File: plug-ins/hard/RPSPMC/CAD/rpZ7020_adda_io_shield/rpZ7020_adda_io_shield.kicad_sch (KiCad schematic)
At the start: 11 parts, among them J1 Samtec_ASP-134486-01

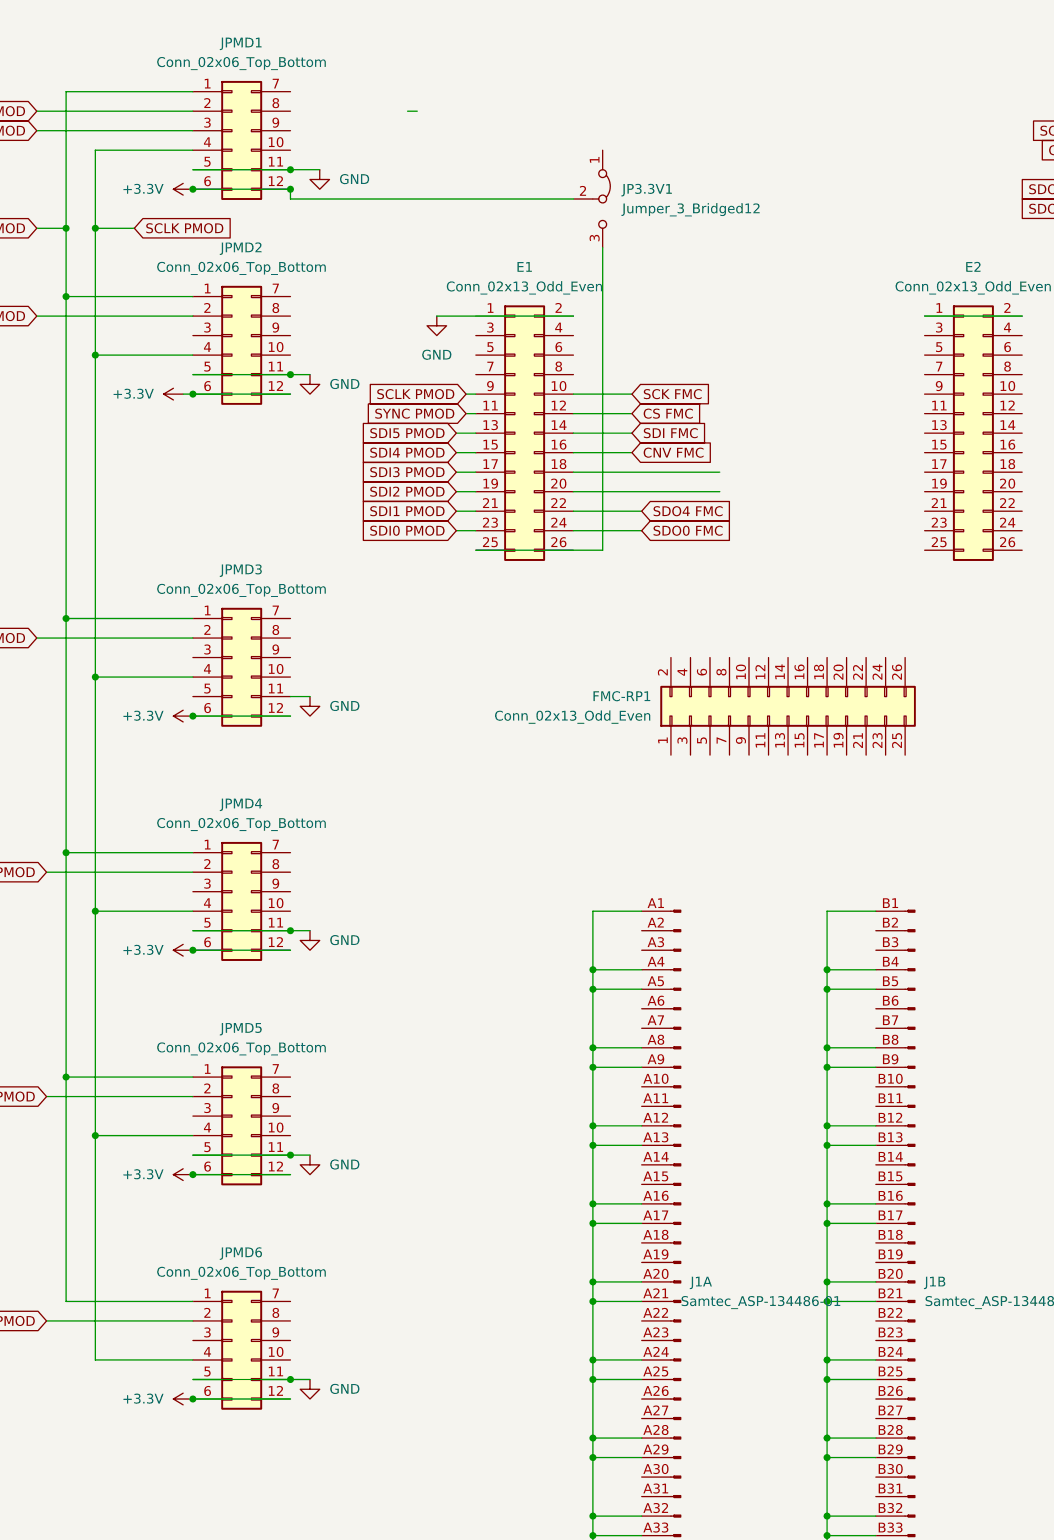
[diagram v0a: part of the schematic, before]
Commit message: profile: auto update axis labels+title from unit MUX: test modes CAD: work on RP hat
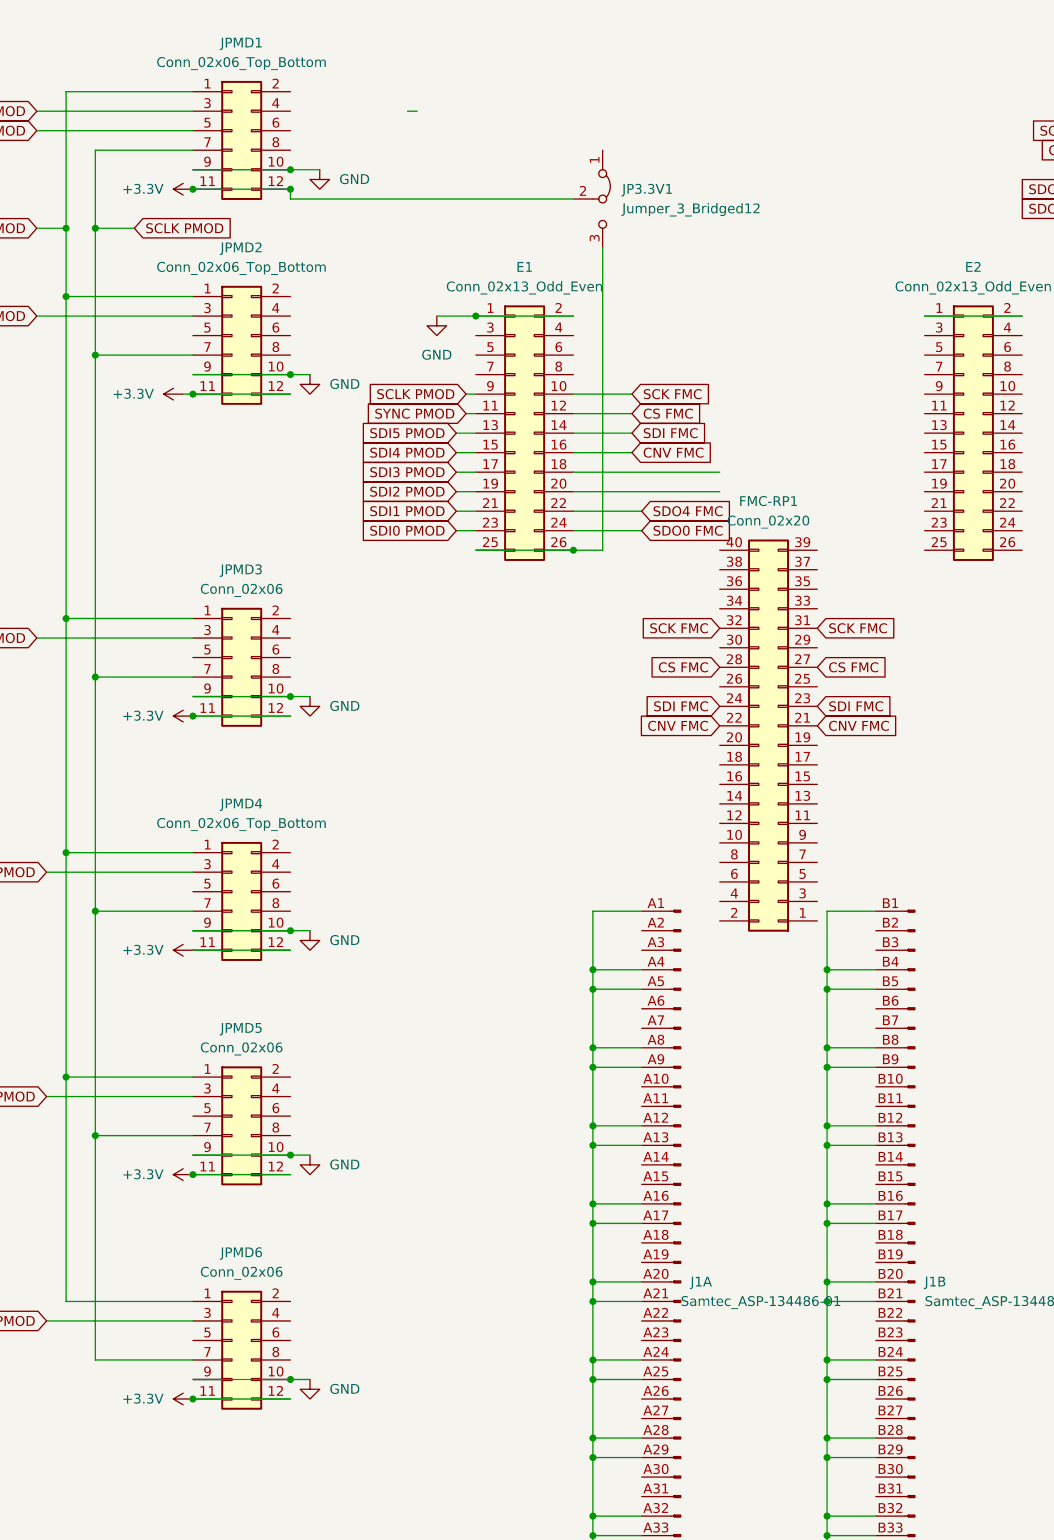
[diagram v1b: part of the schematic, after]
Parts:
- FMC-RP1: value Conn_02x13_Odd_Even -> Conn_02x20; footprint Connector_PinHeader_2.54mm:PinHeader_2x13_P2.54mm_Vertical -> Connector_PinHeader_2.54mm:PinHeader_2x20_P2.54mm_Vertical; symbol Connector_Generic:Conn_02x13_Odd_Even -> Connector_Generic:Conn_02x20_Odd_Even
- JP3.3V1: footprint (none) -> Connector_PinSocket_2.54mm:PinSocket_1x03_P2.54mm_Vertical
- JPMD1, JPMD2, JPMD4: footprint Connector_PinSocket_2.54mm:PinSocket_2x06_P2.54mm_Horizontal -> Connector_PinSocket_2.54mm:PinSocket_2x06_P2.54mm_Vertical; symbol Connector_Generic:Conn_02x06_Top_Bottom -> Connector_Generic:Conn_02x06_Odd_Even
- JPMD3, JPMD5, JPMD6: value Conn_02x06_Top_Bottom -> Conn_02x06; footprint Connector_PinSocket_2.54mm:PinSocket_2x06_P2.54mm_Horizontal -> Connector_PinSocket_2.54mm:PinSocket_2x06_P2.54mm_Vertical; symbol Connector_Generic:Conn_02x06_Top_Bottom -> Connector_Generic:Conn_02x06_Odd_Even
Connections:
- net +3.3V: now also JPMD1.11 (Pin_11), JPMD2.11 (Pin_11), JPMD3.11 (Pin_11), JPMD4.11 (Pin_11), JPMD5.11 (Pin_11), JPMD6.11 (Pin_11); no longer JPMD1.6 (Pin_6), JPMD2.6 (Pin_6), JPMD3.6 (Pin_6), JPMD4.6 (Pin_6), JPMD5.6 (Pin_6), JPMD6.6 (Pin_6)
- net CNV FMC: now also FMC-RP1.21 (Pin_21), FMC-RP1.22 (Pin_22)
- net CS FMC: now also FMC-RP1.27 (Pin_27), FMC-RP1.28 (Pin_28)
- net GND: now also E1.1 (Pin_1), JPMD1.10 (Pin_10), JPMD1.9 (Pin_9), JPMD2.10 (Pin_10), JPMD2.9 (Pin_9), JPMD3.10 (Pin_10), JPMD3.9 (Pin_9), JPMD4.10 (Pin_10), JPMD4.9 (Pin_9), JPMD5.10 (Pin_10), JPMD5.9 (Pin_9), JPMD6.10 (Pin_10), JPMD6.9 (Pin_9); no longer JPMD1.11 (Pin_11), JPMD1.5 (Pin_5), JPMD2.11 (Pin_11), JPMD2.5 (Pin_5), JPMD3.11 (Pin_11), JPMD4.11 (Pin_11), JPMD4.5 (Pin_5), JPMD5.11 (Pin_11), JPMD5.5 (Pin_5), JPMD6.11 (Pin_11), JPMD6.5 (Pin_5)
- net SCK FMC: now also FMC-RP1.31 (Pin_31), FMC-RP1.32 (Pin_32)
- net SCLK PMOD: now also JPMD1.7 (Pin_7), JPMD2.7 (Pin_7), JPMD3.7 (Pin_7), JPMD4.7 (Pin_7), JPMD5.7 (Pin_7), JPMD6.7 (Pin_7); no longer JPMD1.4 (Pin_4), JPMD2.4 (Pin_4), JPMD3.4 (Pin_4), JPMD4.4 (Pin_4), JPMD5.4 (Pin_4), JPMD6.4 (Pin_4)
- net SDI FMC: now also FMC-RP1.23 (Pin_23), FMC-RP1.24 (Pin_24)
- net SDI0 PMOD: now also JPMD1.3 (Pin_3); no longer JPMD1.2 (Pin_2)
- net SDI1 PMOD: now also JPMD2.3 (Pin_3); no longer JPMD2.2 (Pin_2)
- net SDI2 PMOD: now also JPMD3.3 (Pin_3); no longer JPMD3.2 (Pin_2)
- net SDI3 PMOD: now also JPMD4.3 (Pin_3); no longer JPMD4.2 (Pin_2)
- net SDI4 PMOD: now also JPMD5.3 (Pin_3); no longer JPMD5.2 (Pin_2)
- net SDI5 PMOD: now also JPMD6.3 (Pin_3); no longer JPMD6.2 (Pin_2)
- net SDO0 PMOD: now also JPMD1.5 (Pin_5); no longer JPMD1.3 (Pin_3)
- net at E1.25 (Pin_25), JP3.3V1.3 (B): now also E1.26 (Pin_26)

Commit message: work on RP hat
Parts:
- added C1, C2, C3, C4, C5, C6: C, Capacitor_THT:C_Rect_L4.6mm_W2.0mm_P2.50mm_MKS02_FKP02, symbol Device:C
- added J3-FMC-POWER1, J4-FMC-AUX1: Conn_02x06_Odd_Even, Connector_PinHeader_2.54mm:PinHeader_2x06_P2.54mm_Vertical, symbol Connector_Generic:Conn_02x06_Odd_Even
- added R1, R2: 1k, Resistor_SMD:R_0805_2012Metric, symbol Device:R
- JP-EXT-3.3V-RP1: renamed from JP3.3V1; footprint Connector_PinSocket_2.54mm:PinSocket_1x03_P2.54mm_Vertical -> Connector_PinHeader_2.54mm:PinHeader_1x03_P2.54mm_Vertical
- renumbered FMC-RP1 to J2-FMC-RP1
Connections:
- net +12V FMC: now also J3-FMC-POWER1.1 (Pin_1), J3-FMC-POWER1.2 (Pin_2)
- net +3.3V: now also C1.2, C2.2, C3.2, C4.2, C5.2, C6.2
- net A0 EE: now also J4-FMC-AUX1.10 (Pin_10)
- net A1 EE: now also J4-FMC-AUX1.12 (Pin_12)
- net AUX 3.3V EE: now also J3-FMC-POWER1.8 (Pin_8)
- net BUSY FMC: now also J2-FMC-RP1.19 (Pin_19)
- net CLK-ADC: now also J4-FMC-AUX1.1 (Pin_1)
- net CNV FMC: no longer E1.16 (Pin_16), J2-FMC-RP1.22 (Pin_22)
- net CS FMC: now also J2-FMC-RP1.17 (Pin_17); no longer E1.12 (Pin_12), J2-FMC-RP1.27 (Pin_27), J2-FMC-RP1.28 (Pin_28)
- net EN: now also J4-FMC-AUX1.8 (Pin_8)
- net GND: now also E2.1 (Pin_1), E2.15 (Pin_15), E2.2 (Pin_2), E2.5 (Pin_5), E2.6 (Pin_6), C1.1, C2.1, C3.1, C4.1, C5.1, C6.1, J3-FMC-POWER1.11 (Pin_11), J3-FMC-POWER1.3 (Pin_3), J3-FMC-POWER1.4 (Pin_4), J3-FMC-POWER1.5 (Pin_5), J3-FMC-POWER1.6 (Pin_6), J4-FMC-AUX1.11 (Pin_11), J4-FMC-AUX1.3 (Pin_3), J4-FMC-AUX1.4 (Pin_4), J4-FMC-AUX1.5 (Pin_5), J4-FMC-AUX1.6 (Pin_6), J4-FMC-AUX1.9 (Pin_9)
- net RESET FMC: now also J2-FMC-RP1.29 (Pin_29)
- net SCK FMC: now also J2-FMC-RP1.25 (Pin_25); no longer E1.10 (Pin_10), J2-FMC-RP1.31 (Pin_31), J2-FMC-RP1.32 (Pin_32)
- net SCK OUT FMC: now also J2-FMC-RP1.31 (Pin_31)
- net SCL EE: now also J2-FMC-RP1.37 (Pin_37)
- net SDA EE: now also J2-FMC-RP1.39 (Pin_39)
- net SDI FMC: no longer E1.14 (Pin_14), J2-FMC-RP1.24 (Pin_24)
- net SDO0 FMC: now also J2-FMC-RP1.1 (Pin_1); no longer E1.24 (Pin_24)
- net SDO1 FMC: now also J2-FMC-RP1.3 (Pin_3)
- net SDO2 FMC: now also J2-FMC-RP1.5 (Pin_5)
- net SDO3 FMC: now also J2-FMC-RP1.7 (Pin_7)
- net SDO4 FMC: now also J2-FMC-RP1.9 (Pin_9); no longer E1.22 (Pin_22)
- net SDO5 FMC: now also J2-FMC-RP1.11 (Pin_11)
- net SDO6 FMC: now also J2-FMC-RP1.13 (Pin_13)
- net SDO7 FMC: now also J2-FMC-RP1.15 (Pin_15)
- net VADJ: now also J4-FMC-AUX1.2 (Pin_2)
- net D1P RP: now reaches J2-FMC-RP1.10 (Pin_10)
- net D1P RP: now also E1.22 (Pin_22)
- net D3P RP: now reaches J2-FMC-RP1.18 (Pin_18)
- net D3P RP: now also E1.18 (Pin_18)
- net D0P RP: now reaches J2-FMC-RP1.2 (Pin_2)
- net D0P RP: now also E1.24 (Pin_24)
- net D4P RP: now reaches J2-FMC-RP1.20 (Pin_20)
- net D4P RP: now also E1.16 (Pin_16)
- net D7P RP: now reaches J2-FMC-RP1.26 (Pin_26)
- net D7P RP: now also E1.10 (Pin_10)
- net D2P RP: now reaches J2-FMC-RP1.30 (Pin_30)
- net D2P RP: now also E1.20 (Pin_20)
- net I2C SCL RP: now reaches J2-FMC-RP1.38 (Pin_38)
- net I2C SCL RP: now also E2.18 (Pin_18), J3-FMC-POWER1.10 (Pin_10), R2.2
- net I2C SDA RP: now reaches J2-FMC-RP1.40 (Pin_40)
- net I2C SDA RP: now also E2.17 (Pin_17), J3-FMC-POWER1.9 (Pin_9), R1.2
- net RP 3.3V: now reaches JP-EXT-3.3V-RP1.1 (A)
- net RP 3.3V: now also E1.25 (Pin_25), E1.26 (Pin_26), J3-FMC-POWER1.7 (Pin_7), J4-FMC-AUX1.7 (Pin_7), R1.1, R2.1
- net UART RX RP: now reaches E2.19 (Pin_19)
- net UART TX RP: now reaches E2.20 (Pin_20)
- net SPI CS RP: now reaches E2.21 (Pin_21)
- net SPI CLK RP: now reaches E2.22 (Pin_22)
- net MISO RP: now reaches E2.23 (Pin_23)
- net MOSI RP: now reaches E2.24 (Pin_24)
- net RP -4V: now reaches E2.25 (Pin_25)
- net RP 5V: now reaches E2.26 (Pin_26)
- new net D5P RP: E1.14 (Pin_14), J2-FMC-RP1.22 (Pin_22)
- new net D6P RP: E1.12 (Pin_12), J2-FMC-RP1.24 (Pin_24)
- new net EXT 3.3V DAC: J3-FMC-POWER1.12 (Pin_12), JP-EXT-3.3V-RP1.3 (B)
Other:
- moved on the sheet: E2, J1A, J1B, J1E, J1F, J1I, J1J, J2-FMC-RP1, JP-EXT-3.3V-RP1

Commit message: RP hat
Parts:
- E1, E2: now not fitted
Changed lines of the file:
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@@
 		(in_bom yes)
 		(on_board yes)
-		(dnp no)
+		(dnp yes)
 		(fields_autoplaced yes)
 		(property "Reference" "E1"
@@
 		(in_bom yes)
 		(on_board yes)
-		(dnp no)
+		(dnp yes)
 		(fields_autoplaced yes)
 		(property "Reference" "E2"

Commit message: finalizing board, gnd plane, details
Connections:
- net D2P RP: now also J2-FMC-RP1.4 (Pin_4)
- net D3P RP: now also J2-FMC-RP1.12 (Pin_12)
- net GND: now also J2-FMC-RP1.27 (Pin_27), J2-FMC-RP1.28 (Pin_28), J2-FMC-RP1.35 (Pin_35), J2-FMC-RP1.36 (Pin_36)
- net RP 3.3V: now also J2-FMC-RP1.34 (Pin_34)
- net SDO5 PMOD: now reaches JPMD6.5 (Pin_5)
- net SDO4 PMOD: now reaches JPMD5.5 (Pin_5)
- net SDO3 PMOD: now reaches JPMD4.5 (Pin_5)
- net SDO2 PMOD: now reaches JPMD3.5 (Pin_5)
- net SDO1 PMOD: now reaches JPMD2.5 (Pin_5)
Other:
- company: (none) -> PyZahl@BNL
- title: (none) -> RedPitaya HAT for RP-SPMC-GXSM4 Analog Modules

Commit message: work ok hat
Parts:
- added TP-CLK1, TP-GND1, TP-SYNC1: TestPoint, Connector_Pin:Pin_D0.7mm_L6.5mm_W1.8mm_FlatFork, symbol Connector:TestPoint
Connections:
- net GND: now also TP-GND1.1
- net SCLK PMOD: now also TP-CLK1.1
- net SYNC PMOD: now also TP-SYNC1.1
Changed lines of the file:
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@@
 	)
 	(junction
+		(at 30.48 60.96)
+		(diameter 0)
+		(color 0 0 0 0)
+	)
+	(junction
 		(at 181.61 36.83)
 		(diameter 0)
@@
 	)
 	(junction
+		(at 34.29 60.96)
+		(diameter 0)
+		(color 0 0 0 0)
+	)
+	(junction
 		(at 111.76 213.36)
 		(diameter 0)
@@
 	)
 	(junction
+		(at 64.77 21.59)
+		(diameter 0)
+		(color 0 0 0 0)
+	)
+	(junction
 		(at 283.21 153.67)
 		(diameter 0)
@@
 	(wire
 		(pts
+			(xy 30.48 60.96) (xy 30.48 80.01)
+		)
+		(stroke
+			(width 0)
+			(type default)
+		)
+	)
+	(wire
+		(pts
 			(xy 195.58 227.33) (xy 201.93 227.33)
 		)
@@
 	(wire
 		(pts
+			(xy 34.29 60.96) (xy 34.29 87.63)
+		)
+		(stroke
+			(width 0)
+			(type default)
+		)
+	)
+	(wire
+		(pts
 			(xy 299.72 209.55) (xy 299.72 217.17)
 		)
@@
 	(wire
 		(pts
-			(xy 30.48 38.1) (xy 30.48 80.01)
+			(xy 30.48 38.1) (xy 30.48 60.96)
 		)
 		(stroke
@@
 	(wire
 		(pts
-			(xy 34.29 45.72) (xy 34.29 87.63)
+			(xy 34.29 45.72) (xy 34.29 60.96)
 		)
 		(stroke
@@
 	)
 	(symbol
+		(lib_id "Connector:TestPoint")
+		(at 64.77 21.59 270)
+		(unit 1)
+		(exclude_from_sim no)
+		(in_bom yes)
+		(on_board yes)
+		(dnp no)
+		(fields_autoplaced yes)
+		(property "Reference" "TP-GND1"
+			(at 69.85 21.5899 90)
+			(effects
+				(font
+					(size 1.27 1.27)
+				)
+				(justify left)
+			)
+		)
+		(property "Value" "TestPoint"
+			(at 69.85 22.8599 90)
+			(effects
+				(font
+					(size 1.27 1.27)
+				)
+				(justify left)
+				(hide yes)
+			)
+		)
+		(property "Footprint" "Connector_Pin:Pin_D0.7mm_L6.5mm_W1.8mm_FlatFork"
+			(at 64.77 26.67 0)
+			(effects
+				(font
+					(size 1.27 1.27)
+				)
+				(hide yes)
+			)
+		)
+		(property "Datasheet" "~"
+			(at 64.77 26.67 0)
+			(effects
+				(font
+					(size 1.27 1.27)
+				)
+				(hide yes)
+			)
+		)
+		(property "Description" "test point"
+			(at 64.77 21.59 0)
+			(effects
+				(font
+					(size 1.27 1.27)
+				)
+				(hide yes)
+			)
+		)
+		(pin "1"
+		)
+		(instances
+			(project "rpZ7020_adda_io_shield"
+				(path "/63df56e0-33e2-40b2-bbfc-0201c9a11b00"
+					(reference "TP-GND1")
+					(unit 1)
+				)
+			)
+		)
+	)
+	(symbol
 		(lib_id "Connector_Generic:Conn_02x06_Odd_Even")
 		(at 86.36 99.06 0)
@@
 	)
 	(symbol
+		(lib_id "Connector:TestPoint")
+		(at 34.29 60.96 270)
+		(unit 1)
+		(exclude_from_sim no)
+		(in_bom yes)
+		(on_board yes)
+		(dnp no)
+		(fields_autoplaced yes)
+		(property "Reference" "TP-CLK1"
+			(at 39.37 60.9599 90)
+			(effects
+				(font
+					(size 1.27 1.27)
+				)
+				(justify left)
+			)
+		)
+		(property "Value" "TestPoint"
+			(at 39.37 62.2299 90)
+			(effects
+				(font
+					(size 1.27 1.27)
+				)
+				(justify left)
+				(hide yes)
+			)
+		)
+		(property "Footprint" "Connector_Pin:Pin_D0.7mm_L6.5mm_W1.8mm_FlatFork"
+			(at 34.29 66.04 0)
+			(effects
+				(font
+					(size 1.27 1.27)
+				)
+				(hide yes)
+			)
+		)
+		(property "Datasheet" "~"
+			(at 34.29 66.04 0)
+			(effects
+				(font
+					(size 1.27 1.27)
+				)
+				(hide yes)
+			)
+		)
+		(property "Description" "test point"
+			(at 34.29 60.96 0)
+			(effects
+				(font
+					(size 1.27 1.27)
+				)
+				(hide yes)
+			)
+		)
+		(pin "1"
+		)
+		(instances
+			(project ""
+				(path "/63df56e0-33e2-40b2-bbfc-0201c9a11b00"
+					(reference "TP-CLK1")
+					(unit 1)
+				)
+			)
+		)
+	)
+	(symbol
 		(lib_id "power:GND")
 		(at 78.74 40.64 0)
@@
 					(unit 1)
 				)
+			)
+		)
+	)
+	(symbol
+		(lib_id "Connector:TestPoint")
+		(at 30.48 60.96 90)
+		(unit 1)
+		(exclude_from_sim no)
+		(in_bom yes)
+		(on_board yes)
+		(dnp no)
+		(fields_autoplaced yes)
+		(property "Reference" "TP-SYNC1"
+			(at 27.178 58.42 90)
+			(effects
+				(font
+					(size 1.27 1.27)
+				)
+			)
+		)
+		(property "Value" "TestPoint"
+			(at 27.178 58.42 90)
+			(effects
+				(font
+					(size 1.27 1.27)
+				)
+				(hide yes)
+			)
+		)
+		(property "Footprint" "Connector_Pin:Pin_D0.7mm_L6.5mm_W1.8mm_FlatFork"
+			(at 30.48 55.88 0)
+			(effects
+				(font
+					(size 1.27 1.27)
+				)
+				(hide yes)
+			)
+		)
+		(property "Datasheet" "~"
+			(at 30.48 55.88 0)
+			(effects
+				(font
+					(size 1.27 1.27)
+				)
+				(hide yes)
+			)
+		)
+		(property "Description" "test point"
+			(at 30.48 60.96 0)
+			(effects
+				(font
+					(size 1.27 1.27)
+				)
+				(hide yes)
+			)
+		)
+		(pin "1"
+		)
+		(instances
+			(project "rpZ7020_adda_io_shield"
+				(path "/63df56e0-33e2-40b2-bbfc-0201c9a11b00"
+					(reference "TP-SYNC1")
+					(unit 1)
+				)
